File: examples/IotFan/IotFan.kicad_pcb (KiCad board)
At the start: 2 copper layers, 30 x 80 mm, 83 parts

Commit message: Update IotFan.kicad_pcb
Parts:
- moved prot_3v3 35.4 mm to (83.0, 132.0)
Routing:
- net Fv12_sense.output: track 2.46 -> 4.31 mm, vias 1 -> 2
- net Fv12: track 135.2 -> 134.5 mm
- net Fv3v3: track 81.2 -> 80.6 mm, vias 6 -> 8
- net Fgnd: track 25.3 -> 25.5 mm, vias 20 -> 21

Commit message: Update IotFan.kicad_pcb
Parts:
- moved prot_3v3 24.4 mm to (106.0, 124.0)
- turned enc to 90 degrees
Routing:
- net Fv3v3: track 80.6 -> 122.2 mm, vias 8 -> 11
- net Fmcu.program_boot_node: track 2.33 -> 37.6 mm, vias 2 -> 4
- net Fmcu.program_en_node: track 10.1 -> 44.5 mm, vias 3 -> 2
- net Fmcu.program_uart_node.a_tx: track 2.47 -> 27.2 mm
- net Ffan_ctl[0].control: track 27.7 -> 3.46 mm, vias 4 -> 1
- net Fmcu.program_uart_node.b_tx: track 2.82 -> 24.2 mm
- net (no net): track 20.9 -> 0.00 mm, vias 3 -> 0
- net Fv5: track 133.1 -> 149.6 mm, vias 1 -> 2
- net Fv12_sense.output: track 4.31 -> 16.1 mm
- net Fenc.a: track 1.66 -> 12.2 mm
- net Freg_5v.fb.output: track 2.96 -> 11.7 mm
- net Fenc.b: track 1.23 -> 8.77 mm
- net Fenc.sw: track 1.21 -> 7.25 mm
- net Ffan_drv[0].control: track 1.84 -> 6.96 mm
- net Fv12: track 134.5 -> 137.5 mm, vias 8 -> 12
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
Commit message: wip
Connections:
- ledr.package pad 2: Fv3v3 -> Fledr.signal
- mcu.ic pad 6: Fv3v3 -> Fledr.signal
- rgb_ring.led[0] pad 1: Fv3v3 -> Fledr.signal
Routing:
- net Fv3v3: track 122.2 -> 93.5 mm, vias 11 -> 8
- net Fledr.signal: track 0.00 -> 28.7 mm, vias 0 -> 3
- net Fgnd: vias 31 -> 30
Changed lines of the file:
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@@
   (net 51 "Frgb_ring.led[14].dout")
   (net 52 "Fmcu.pi.output")
+  (net 53 "Fledr.signal")
   (footprint "edg:TestPoint_TE_RCT_0805" (layer "F.Cu")
     (at 93 139 180)
@@
       (net 5 "Fenc.a"))
     (pad "6" smd roundrect (at -2.475 0.75 135) (size 0.75 0.25) (layers "F.Cu" "F.Paste" "F.Mask") (roundrect_rratio 0.25)
-      (net 4 "Fv3v3"))
+      (net 53 "Fledr.signal"))
     (pad "7" smd roundrect (at -2.475 1.25 135) (size 0.75 0.25) (layers "F.Cu" "F.Paste" "F.Mask") (roundrect_rratio 0.25)
       (net 10 "Fmcu.program_en_node"))
@@
       (net 13 "Fledr.res.a"))
     (pad "2" smd roundrect (at 0.7875 0 135) (size 0.875 0.95) (layers "F.Cu" "F.Paste" "F.Mask") (roundrect_rratio 0.25)
-      (net 4 "Fv3v3"))
+      (net 53 "Fledr.signal"))
     (model "${KICAD6_3DMODEL_DIR}/LED_SMD.3dshapes/LED_0603_1608Metric.wrl"
       (offset (xyz 0 0 0))
@@
       (stroke (width 0.1) (type solid)) (fill solid) (layer "F.Fab"))
     (pad "1" smd rect (at -0.45 -0.45 80) (size 0.5 0.5) (layers "F.Cu" "F.Paste" "F.Mask")
-      (net 4 "Fv3v3"))
+      (net 53 "Fledr.signal"))
     (pad "2" smd rect (at -0.45 0.45 80) (size 0.5 0.5) (layers "F.Cu" "F.Paste" "F.Mask")
       (net 3 "Fv5"))
@@
   (via (at 110 128) (size 0.7) (drill 0.3) (layers "F.Cu" "B.Cu") (net 2))
   (via (at 112 129) (size 0.7) (drill 0.3) (layers "F.Cu" "B.Cu") (net 2))
-  (via (at 100 103) (size 0.9) (drill 0.5) (layers "F.Cu" "B.Cu") (net 2))
   (via (at 104 76) (size 0.9) (drill 0.5) (layers "F.Cu" "B.Cu") (net 2))
   (via (at 113 133) (size 0.7) (drill 0.3) (layers "F.Cu" "B.Cu") (net 2))
@@
   (segment (start 112 114.775) (end 111.225 114.775) (width 0.2) (layer "F.Cu") (net 4))
   (segment (start 109 126) (end 109 123.474874) (width 0.2) (layer "F.Cu") (net 4))
-  (segment (start 100 130) (end 100 134) (width 0.16) (layer "F.Cu") (net 4))
   (segment (start 114 127.225) (end 113.225 127.225) (width 0.5) (layer "F.Cu") (net 4))
   (segment (start 106 116.775) (end 106.775 116.775) (width 0.2) (layer "F.Cu") (net 4))
@@
   (segment (start 106 126) (end 106 127.05) (width 0.5) (layer "F.Cu") (net 4))
   (segment (start 109.275 114.775) (end 110 114.775) (width 0.2) (layer "F.Cu") (net 4))
-  (segment (start 112.280419 121.219759) (end 113 121.93934) (width 0.16) (layer "F.Cu") (net 4))
   (segment (start 113.25 117.81066) (end 112.280419 118.780241) (width 0.2) (layer "F.Cu") (net 4))
   (segment (start 113 115) (end 113.25 115.25) (width 0.2) (layer "F.Cu") (net 4))
@@
   (segment (start 106 126) (end 106 125.05) (width 0.5) (layer "F.Cu") (net 4))
   (segment (start 113.25 115.25) (end 113.25 116.75) (width 0.2) (layer "F.Cu") (net 4))
-  (segment (start 113 121.93934) (end 113 122) (width 0.16) (layer "F.Cu") (net 4))
   (segment (start 106.775 116.775) (end 107 117) (width 0.2) (layer "F.Cu") (net 4))
   (segment (start 113.225 127.225) (end 113 127) (width 0.5) (layer "F.Cu") (net 4))
@@
   (segment (start 87.050987 135.550987) (end 87.652962 135.550987) (width 0.5) (layer "F.Cu") (net 4))
   (segment (start 107 117) (end 108.5 117) (width 0.2) (layer "F.Cu") (net 4))
-  (via (at 100 134) (size 0.7) (drill 0.3) (layers "F.Cu" "B.Cu") (net 4))
-  (via (at 100 130) (size 0.7) (drill 0.3) (layers "F.Cu" "B.Cu") (net 4))
   (via (at 88 129) (size 0.9) (drill 0.5) (layers "F.Cu" "B.Cu") (net 4))
   (via (at 113 127) (size 0.7) (drill 0.3) (layers "F.Cu" "B.Cu") (net 4))
@@
   (via (at 103 129) (size 0.9) (drill 0.5) (layers "F.Cu" "B.Cu") (net 4))
   (via (at 88 130) (size 0.9) (drill 0.5) (layers "F.Cu" "B.Cu") (net 4))
-  (via (at 113 122) (size 0.7) (drill 0.3) (layers "F.Cu" "B.Cu") (net 4))
   (via (at 106 126) (size 0.7) (drill 0.3) (layers "F.Cu" "B.Cu") (net 4))
   (segment (start 106 126) (end 107 126) (width 0.5) (layer "B.Cu") (net 4))
   (segment (start 114.75 125.25) (end 113 127) (width 0.2) (layer "B.Cu") (net 4))
-  (segment (start 113 122) (end 113.5 122.5) (width 0.16) (layer "B.Cu") (net 4))
   (segment (start 112 126) (end 113 127) (width 0.5) (layer "B.Cu") (net 4))
   (segment (start 107 126) (end 112 126) (width 0.5) (layer "B.Cu") (net 4))
@@
   (segment (start 109 126) (end 107 126) (width 0.5) (layer "B.Cu") (net 4))
   (segment (start 88 129) (end 97 129) (width 0.5) (layer "B.Cu") (net 4))
-  (segment (start 113.5 124.25) (end 113 124.75) (width 0.16) (layer "B.Cu") (net 4))
-  (segment (start 113.5 122.5) (end 113.5 124.25) (width 0.16) (layer "B.Cu") (net 4))
   (segment (start 103 129) (end 106 126) (width 0.5) (layer "B.Cu") (net 4))
   (segment (start 114.75 125.25) (end 114.75 122.75) (width 0.16) (layer "B.Cu") (net 4))
-  (segment (start 113 124.75) (end 104.75 124.75) (width 0.16) (layer "B.Cu") (net 4))
   (segment (start 114.75 122.75) (end 114.75 121.5) (width 0.2) (layer "B.Cu") (net 4))
-  (segment (start 104.75 124.75) (end 100 129.5) (width 0.16) (layer "B.Cu") (net 4))
-  (segment (start 100 134) (end 96.5 137.5) (width 0.16) (layer "B.Cu") (net 4))
   (segment (start 88 130) (end 88 129) (width 0.5) (layer "B.Cu") (net 4))
-  (segment (start 100 129.5) (end 100 130) (width 0.16) (layer "B.Cu") (net 4))
   (segment (start 111.926866 121.573313) (end 112.25 121.896447) (width 0.16) (layer "F.Cu") (net 5))
   (segment (start 112.25 122.25) (end 112.5 122.5) (width 0.16) (layer "F.Cu") (net 5))
@@
   (segment (start 112 132.7875) (end 112 134.020102) (width 0.2) (layer "F.Cu") (net 52))
   (segment (start 110 132.775) (end 111.9875 132.775) (width 0.2) (layer "F.Cu") (net 52))
+  (segment (start 100 130) (end 100 134) (width 0.16) (layer "F.Cu") (net 53))
+  (segment (start 112.280419 121.219759) (end 113 121.93934) (width 0.16) (layer "F.Cu") (net 53))
+  (segment (start 113 121.93934) (end 113 122) (width 0.16) (layer "F.Cu") (net 53))
+  (via (at 100 134) (size 0.7) (drill 0.3) (layers "F.Cu" "B.Cu") (net 53))
+  (via (at 100 130) (size 0.7) (drill 0.3) (layers "F.Cu" "B.Cu") (net 53))
+  (via (at 113 122) (size 0.7) (drill 0.3) (layers "F.Cu" "B.Cu") (net 53))
+  (segment (start 113 122) (end 113.5 122.5) (width 0.16) (layer "B.Cu") (net 53))
+  (segment (start 113.5 124.25) (end 113 124.75) (width 0.16) (layer "B.Cu") (net 53))
+  (segment (start 113.5 122.5) (end 113.5 124.25) (width 0.16) (layer "B.Cu") (net 53))
+  (segment (start 113 124.75) (end 104.75 124.75) (width 0.16) (layer "B.Cu") (net 53))
+  (segment (start 104.75 124.75) (end 100 129.5) (width 0.16) (layer "B.Cu") (net 53))
+  (segment (start 100 134) (end 96.5 137.5) (width 0.16) (layer "B.Cu") (net 53))
+  (segment (start 100 129.5) (end 100 130) (width 0.16) (layer "B.Cu") (net 53))
   (zone (net 2) (net_name "Fgnd") (layers "F&B.Cu") (hatch edge 0.508)
     (connect_pads (clearance 0.254))

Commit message: cleaning
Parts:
- moved tp_gnd 27.9 mm to (86.0, 112.0), turned to -90 degrees
- moved tp_pwr 16.3 mm to (98.0, 123.0)
- moved ledr.res 13.0 mm to (93.0, 139.0), turned to 0 degrees
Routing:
- net Fv12: track 137.5 -> 111.4 mm, vias 12 -> 4
- net Fledr.res.a: track 19.1 -> 4.92 mm, vias 2 -> 0
- net Fgnd: track 27.5 -> 25.7 mm, vias 30 -> 28

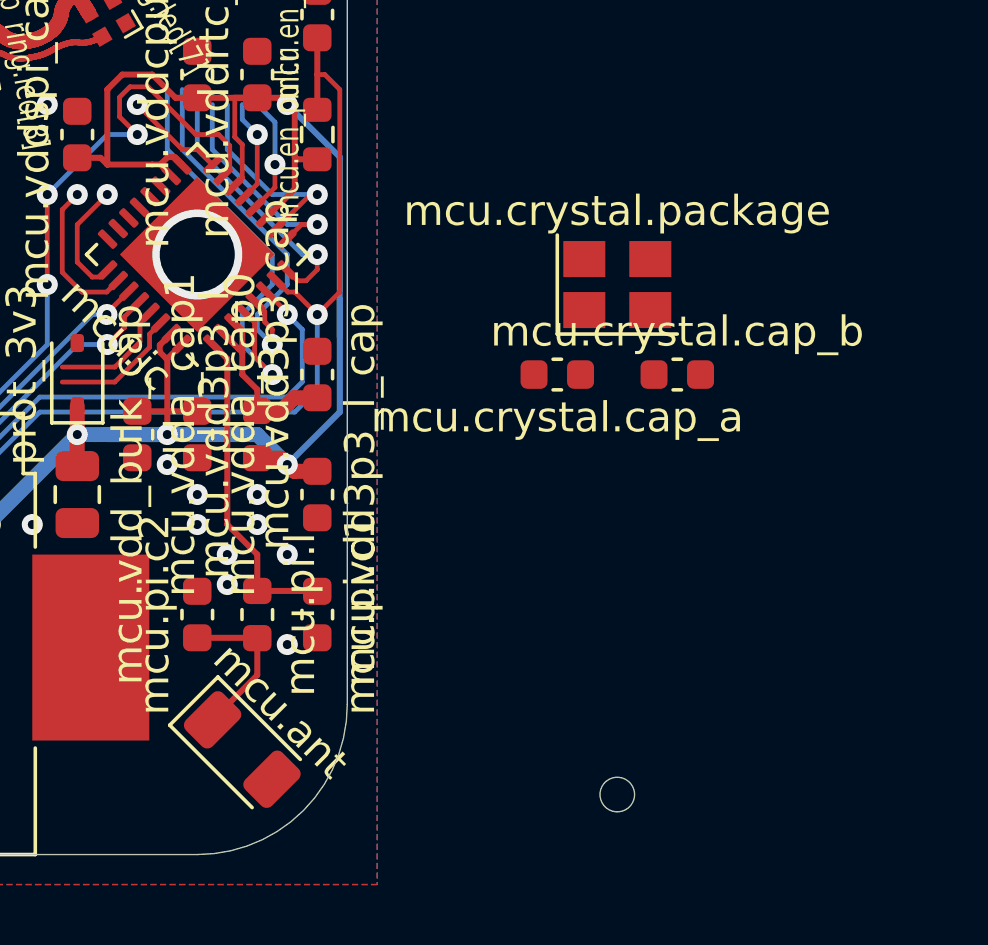
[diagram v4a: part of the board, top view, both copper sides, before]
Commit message: wip smaller xtal
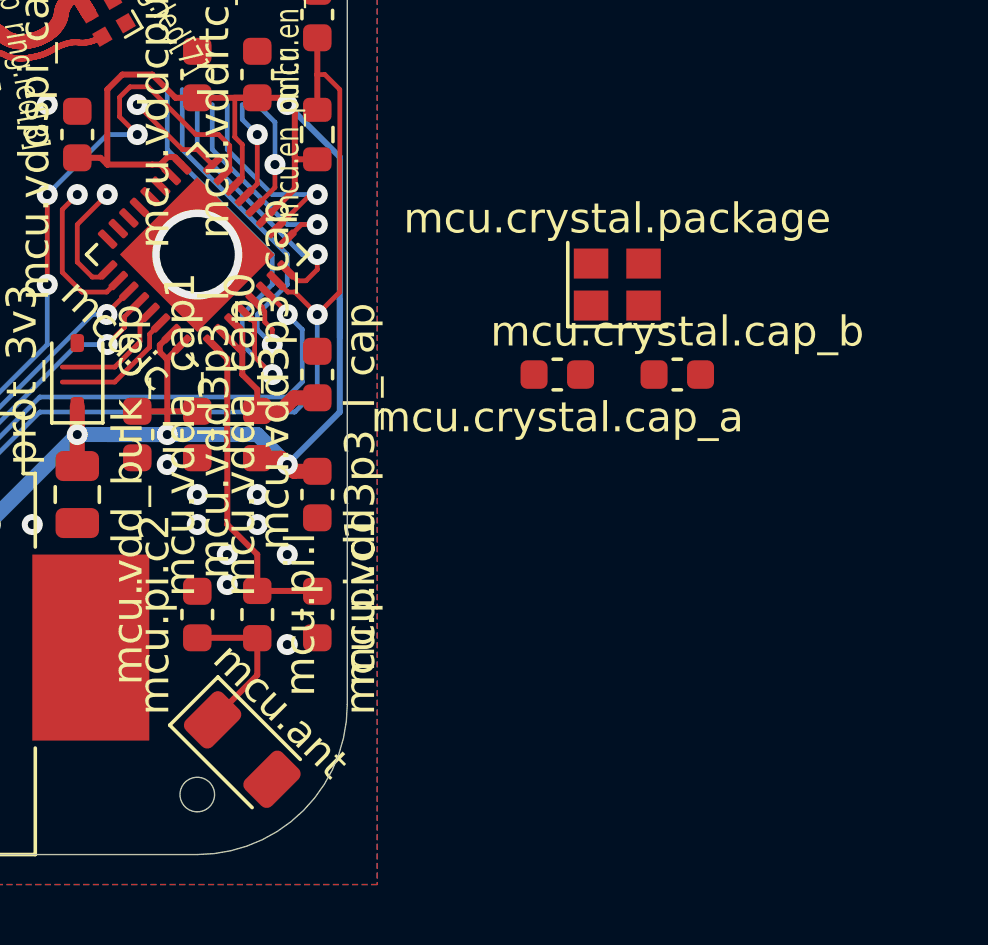
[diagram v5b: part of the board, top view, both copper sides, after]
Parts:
- mcu.crystal.package: value (none) -> TXM40M0004252HBCEO00T (TAE(Zhejiang Abel Elec)) - SMD2520-4P Crystals ROHS; footprint Crystal:Crystal_SMD_3225-4Pin_3.2x2.5mm -> Crystal:Crystal_SMD_2520-4Pin_2.5x2.0mm
- moved jlc_th.th1 14.0 mm to (110.0, 138.0)
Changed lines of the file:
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@@
   )
   (footprint "edg:JlcToolingHole_1.152mm" (layer "F.Cu")
-    (at 124 138)
+    (at 110 138)
     (descr "Tooling holes for JLC assembly, 1.152 mm hole + 1.3mm soldermask opening")
     (property "Sheetfile" "edg.BoardTop.JlcToolingHoles")
@@
     )
   )
-  (footprint "Crystal:Crystal_SMD_3225-4Pin_3.2x2.5mm" (layer "F.Cu")
+  (footprint "Crystal:Crystal_SMD_2520-4Pin_2.5x2.0mm" (layer "F.Cu")
     (at 124 121)
-    (descr "SMD Crystal SERIES SMD3225/4 http://www.txccrystal.com/images/pdf/7m-accuracy.pdf, 3.2x2.5mm^2 package")
+    (descr "SMD Crystal SERIES SMD2520/4 http://www.newxtal.com/UploadFiles/Images/2012-11-12-09-29-09-776.pdf, 2.5x2.0mm^2 package")
     (tags "SMD SMT crystal")
     (property "Sheetfile" "electronics_abstract_parts.AbstractCrystal.OscillatorCrystal")
     (property "Sheetname" "crystal")
-    (property "edg_part" "X322540MPB4SI (Yangxing Tech)")
+    (property "edg_part" "TXM40M0004252HBCEO00T (TAE(Zhejiang Abel Elec))")
     (property "edg_path" "mcu.crystal.package")
     (property "edg_refdes" "FX1")
     (property "edg_short_path" "mcu.crystal.package")
     (attr smd)
-    (fp_text reference "mcu.crystal.package" (at 0 -2.45) (layer "F.SilkS")
-        (effects (font (size 1 1) (thickness 0.15)))
-    )
-    (fp_text value "" (at 0 2.45) (layer "F.Fab")
+    (fp_text reference "mcu.crystal.package" (at 0 -2.2) (layer "F.SilkS")
+        (effects (font (size 1 1) (thickness 0.15)))
+    )
+    (fp_text value "TXM40M0004252HBCEO00T (TAE(Zhejiang Abel Elec)) - SMD2520-4P Crystals ROHS" (at 0 2.2) (layer "F.Fab")
         (effects (font (size 1 1) (thickness 0.15)))
     )
     (fp_text user "${REFERENCE}" (at 0 0) (layer "F.Fab")
-        (effects (font (size 0.7 0.7) (thickness 0.105)))
-    )
-    (fp_line (start -2 -1.65) (end -2 1.65)
-      (stroke (width 0.12) (type solid)) (layer "F.SilkS"))
-    (fp_line (start -2 1.65) (end 2 1.65)
-      (stroke (width 0.12) (type solid)) (layer "F.SilkS"))
-    (fp_line (start -2.1 -1.7) (end -2.1 1.7)
-      (stroke (width 0.05) (type solid)) (layer "F.CrtYd"))
-    (fp_line (start -2.1 1.7) (end 2.1 1.7)
-      (stroke (width 0.05) (type solid)) (layer "F.CrtYd"))
-    (fp_line (start 2.1 -1.7) (end -2.1 -1.7)
-      (stroke (width 0.05) (type solid)) (layer "F.CrtYd"))
-    (fp_line (start 2.1 1.7) (end 2.1 -1.7)
-      (stroke (width 0.05) (type solid)) (layer "F.CrtYd"))
-    (fp_line (start -1.6 -1.25) (end -1.6 1.25)
-      (stroke (width 0.1) (type solid)) (layer "F.Fab"))
-    (fp_line (start -1.6 0.25) (end -0.6 1.25)
-      (stroke (width 0.1) (type solid)) (layer "F.Fab"))
-    (fp_line (start -1.6 1.25) (end 1.6 1.25)
-      (stroke (width 0.1) (type solid)) (layer "F.Fab"))
-    (fp_line (start 1.6 -1.25) (end -1.6 -1.25)
-      (stroke (width 0.1) (type solid)) (layer "F.Fab"))
-    (fp_line (start 1.6 1.25) (end 1.6 -1.25)
-      (stroke (width 0.1) (type solid)) (layer "F.Fab"))
-    (pad "1" smd rect (at -1.1 0.85) (size 1.4 1.2) (layers "F.Cu" "F.Paste" "F.Mask")
+        (effects (font (size 0.6 0.6) (thickness 0.09)))
+    )
+    (fp_line (start -1.65 -1.4) (end -1.65 1.4)
+      (stroke (width 0.12) (type solid)) (layer "F.SilkS"))
+    (fp_line (start -1.65 1.4) (end 1.65 1.4)
+      (stroke (width 0.12) (type solid)) (layer "F.SilkS"))
+    (fp_line (start -1.7 -1.5) (end -1.7 1.5)
+      (stroke (width 0.05) (type solid)) (layer "F.CrtYd"))
+    (fp_line (start -1.7 1.5) (end 1.7 1.5)
+      (stroke (width 0.05) (type solid)) (layer "F.CrtYd"))
+    (fp_line (start 1.7 -1.5) (end -1.7 -1.5)
+      (stroke (width 0.05) (type solid)) (layer "F.CrtYd"))
+    (fp_line (start 1.7 1.5) (end 1.7 -1.5)
+      (stroke (width 0.05) (type solid)) (layer "F.CrtYd"))
+    (fp_line (start -1.25 -0.9) (end -1.15 -1)
+      (stroke (width 0.1) (type solid)) (layer "F.Fab"))
+    (fp_line (start -1.25 0) (end -0.25 1)
+      (stroke (width 0.1) (type solid)) (layer "F.Fab"))
+    (fp_line (start -1.25 0.9) (end -1.25 -0.9)
+      (stroke (width 0.1) (type solid)) (layer "F.Fab"))
+    (fp_line (start -1.15 -1) (end 1.15 -1)
+      (stroke (width 0.1) (type solid)) (layer "F.Fab"))
+    (fp_line (start -1.15 1) (end -1.25 0.9)
+      (stroke (width 0.1) (type solid)) (layer "F.Fab"))
+    (fp_line (start 1.15 -1) (end 1.25 -0.9)
+      (stroke (width 0.1) (type solid)) (layer "F.Fab"))
+    (fp_line (start 1.15 1) (end -1.15 1)
+      (stroke (width 0.1) (type solid)) (layer "F.Fab"))
+    (fp_line (start 1.25 -0.9) (end 1.25 0.9)
+      (stroke (width 0.1) (type solid)) (layer "F.Fab"))
+    (fp_line (start 1.25 0.9) (end 1.15 1)
+      (stroke (width 0.1) (type solid)) (layer "F.Fab"))
+    (pad "1" smd rect (at -0.875 0.7) (size 1.15 1) (layers "F.Cu" "F.Paste" "F.Mask")
       (net 33 "Fmcu.xtal_node.driver.xtal_in"))
-    (pad "2" smd rect (at 1.1 0.85) (size 1.4 1.2) (layers "F.Cu" "F.Paste" "F.Mask")
-      (net 2 "Fgnd"))
-    (pad "3" smd rect (at 1.1 -0.85) (size 1.4 1.2) (layers "F.Cu" "F.Paste" "F.Mask")
+    (pad "2" smd rect (at 0.875 0.7) (size 1.15 1) (layers "F.Cu" "F.Paste" "F.Mask")
+      (net 2 "Fgnd"))
+    (pad "3" smd rect (at 0.875 -0.7) (size 1.15 1) (layers "F.Cu" "F.Paste" "F.Mask")
       (net 32 "Fmcu.xtal_node.driver.xtal_out"))
-    (pad "4" smd rect (at -1.1 -0.85) (size 1.4 1.2) (layers "F.Cu" "F.Paste" "F.Mask")
-      (net 2 "Fgnd"))
-    (model "${KICAD6_3DMODEL_DIR}/Crystal.3dshapes/Crystal_SMD_3225-4Pin_3.2x2.5mm.wrl"
-      (offset (xyz 0 0 0))
-      (scale (xyz 1 1 1))
+    (pad "4" smd rect (at -0.875 -0.7) (size 1.15 1) (layers "F.Cu" "F.Paste" "F.Mask")
+      (net 2 "Fgnd"))
+    (model "${KICAD6_3DMODEL_DIR}/Crystal.3dshapes/Crystal_SMD_2520-4Pin_2.5x2.0mm.wrl"
+      (offset (xyz 0 0 0))
+      (scale (xyz 1 1 1))

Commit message: kinda looking reasonable
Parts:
- moved mcu.crystal.package 23.1 mm to (101.0, 119.0), turned to 90 degrees
- moved mcu.crystal.cap_b 23.0 mm to (103.5, 119.0), turned to -90 degrees
- moved mcu.crystal.cap_a 18.5 mm to (103.5, 123.0), turned to 90 degrees
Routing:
- net Ffan[1].sense: track 3.98 -> 14.6 mm
- net Fmcu.xtal_node.driver.xtal_out: track 4.06 -> 14.2 mm
- net Ffan_ctl[1].control: track 7.06 -> 16.1 mm
- net Fmcu.xtal_node.driver.xtal_in: track 4.35 -> 12.2 mm
- net Fv12: track 111.4 -> 114.5 mm
- net Fgnd: track 25.7 -> 28.2 mm, vias 28 -> 33
- net Ffan_drv[1].control: track 5.30 -> 7.51 mm

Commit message: DONE WOOHOO
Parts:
- renumbered mcu.ant to FANT1, reg_5v.hf_in_cap to FC1, mcu.vddrtc_cap to FC10, mcu.vddcpu_cap to FC11, mcu.vddspi_cap to FC12, mcu.pi.c1 to FC13, mcu.pi.c2 to FC14, mcu.vdd3p3_l_cap to FC15, mcu.vdd3p3_cap to FC16, mcu.crystal.cap_a to FC17, mcu.crystal.cap_b to FC18, mcu.en_pull.c to FC19, reg_5v.boot_cap to FC2, reg_5v.power_path.in_cap to FC3, reg_5v.power_path.out_cap to FC4, reg_3v3.in_cap to FC5, reg_3v3.out_cap to FC6, mcu.vdd_bulk_cap to FC7, mcu.vdda_cap0 to FC8, mcu.vdda_cap1 to FC9, prot_5v to FD1, rgb_ring.led[6] to FD10, rgb_ring.led[7] to FD11, rgb_ring.led[8] to FD12, rgb_ring.led[9] to FD13, rgb_ring.led[10] to FD14, rgb_ring.led[11] to FD15, rgb_ring.led[12] to FD16, rgb_ring.led[13] to FD17, rgb_ring.led[14] to FD18, rgb_ring.led[15] to FD19, prot_3v3 to FD2, rgb_ring.led[16] to FD20, rgb_ring.led[17] to FD21, ledr.package to FD3, rgb_ring.led[0] to FD4, rgb_ring.led[1] to FD5, rgb_ring.led[2] to FD6, rgb_ring.led[3] to FD7, rgb_ring.led[4] to FD8, rgb_ring.led[5] to FD9, jlc_th.th1 to FH1, jlc_th.th2 to FH2, jlc_th.th3 to FH3, pwr to FJ1, mcu.prog to FJ2, fan[0] to FJ3, fan[1] to FJ4, reg_5v.power_path.inductor to FL1, mcu.pi.l to FL2, mcu.vdd3p3_l to FL3, fan_drv[0].pre to FQ1, fan_drv[0].drv to FQ2, fan_ctl[0] to FQ3, fan_drv[1].pre to FQ4, fan_drv[1].drv to FQ5, fan_ctl[1] to FQ6, reg_5v.fb.top_res to FR1, reg_5v.fb.bottom_res to FR2, reg_5v.en_res to FR3, mcu.en_pull.r to FR4, ledr.res to FR5, v12_sense.top_res to FR6, v12_sense.bottom_res to FR7, fan_drv[0].pull to FR8, fan_drv[1].pull to FR9, enc to FSW1, tp_pwr to FTP1, tp_gnd to FTP2, tp_5v to FTP3, tp_3v3 to FTP4, reg_5v.ic to FU1, reg_3v3.ic to FU2, mcu.ic to FU3, mcu.crystal.package to FX1
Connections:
- FU3 pad 10: Ffan_drv[0].control -> Ffan_drv[1].control
- FU3 pad 12: Ffan[0].sense -> Ffan[1].sense
- FU3 pad 13: Ffan_ctl[0].control -> Ffan_ctl[1].control
- FU3 pad 16: Ffan_drv[1].control -> Fenc.b
- FU3 pad 25: Ffan[1].sense -> Fenc.sw
- FU3 pad 26: Ffan_ctl[1].control -> Fenc.a
- FU3 pad 5: Fenc.a -> Ffan_drv[0].control
- FU3 pad 8: Fenc.b -> Ffan_ctl[0].control
- FU3 pad 9: Fenc.sw -> Ffan[0].sense
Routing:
- net Fledr.signal: track 28.7 -> 101.8 mm, vias 3 -> 5
- net Ffan_ctl[0].control: track 3.46 -> 61.6 mm, vias 1 -> 2
- net Ffan_drv[0].control: track 6.96 -> 63.0 mm, vias 1 -> 2
- net Ffan[0].sense: track 3.95 -> 59.3 mm
- net Ffan_drv[1].control: track 7.51 -> 47.1 mm
- net Ffan[1].sense: track 14.6 -> 52.2 mm
- net Ffan_ctl[1].control: track 16.1 -> 48.4 mm
- net Fenc.sw: track 7.25 -> 36.9 mm, vias 1 -> 2
- net Fv12_sense.output: track 16.1 -> 34.0 mm, vias 2 -> 4
- net Fv12: track 114.5 -> 128.8 mm, vias 4 -> 8
- net Fenc.a: track 12.2 -> 23.1 mm, vias 1 -> 2
- net Fenc.b: track 8.77 -> 16.2 mm, vias 1 -> 2
- net Fgnd: track 28.2 -> 26.2 mm, vias 33 -> 31
- net Fv3v3: track 93.5 -> 95.2 mm
- net Fv5: track 149.6 -> 150.2 mm

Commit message: actually done?
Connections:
- FD3 pad 2: Fledr.signal -> Fv3v3
- FD4 pad 1: Fledr.signal -> Frgb_ring.din
- FR5 pad 2: Fgnd -> Fmcu.program_boot_node
- FU3 pad 6: Fledr.signal -> Frgb_ring.din
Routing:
- net Fledr.signal: track 101.8 -> 0.00 mm, vias 5 -> 0
- net Frgb_ring.din: track 0.00 -> 83.8 mm, vias 0 -> 4
- net Fmcu.program_boot_node: track 37.6 -> 53.1 mm, vias 4 -> 5
- net Fv12: track 128.8 -> 133.6 mm
- net Fv3v3: track 95.2 -> 98.2 mm
- net Ffan_drv[0].control: track 63.0 -> 65.9 mm
- net Ffan[1].sense: track 52.2 -> 51.7 mm
- net Fgnd: vias 31 -> 37
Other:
- board text added: "EDG IoT Fan Oct 23 rv2"
- board text removed: "EDG IoT Fan Jul 23 rv1"
